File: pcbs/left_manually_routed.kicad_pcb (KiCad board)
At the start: 2 copper layers, 123.2 x 93.2 mm, 27 parts

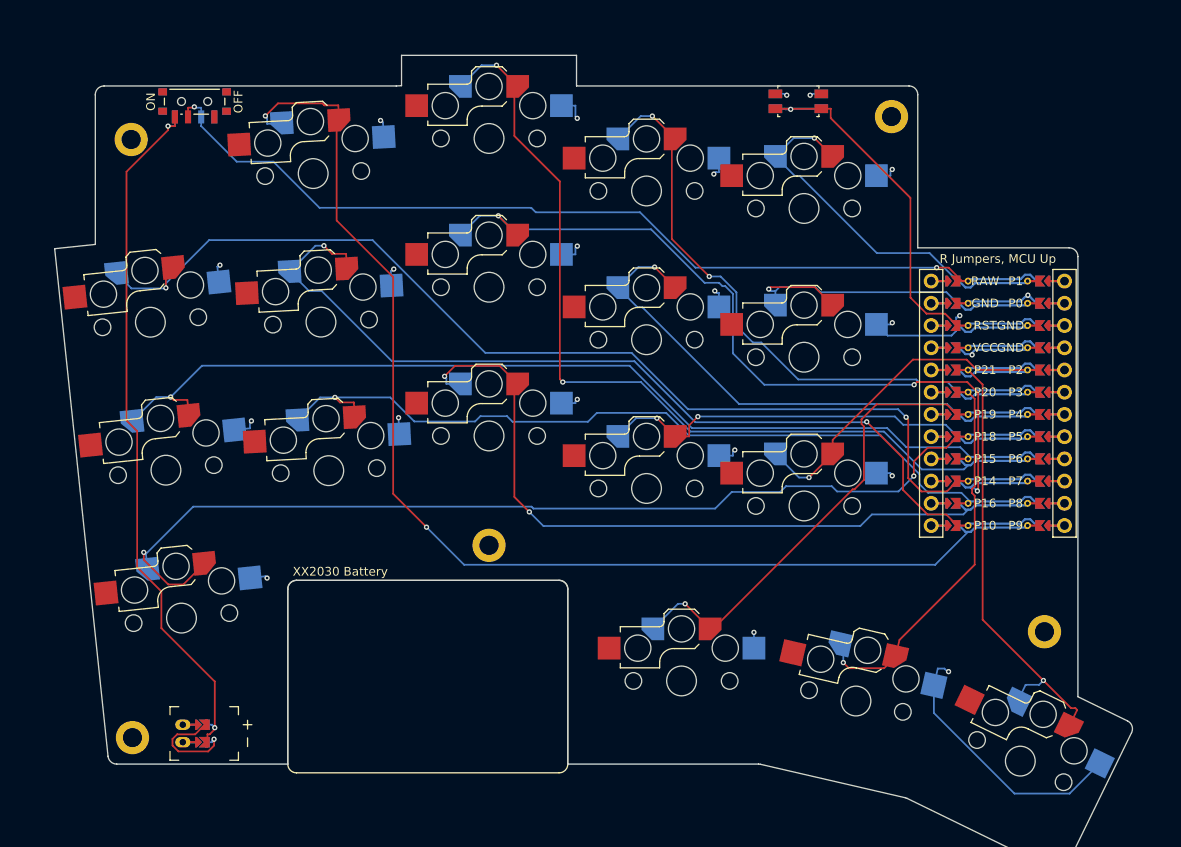
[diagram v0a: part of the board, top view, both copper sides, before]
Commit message: Update manually routed pcb and export model
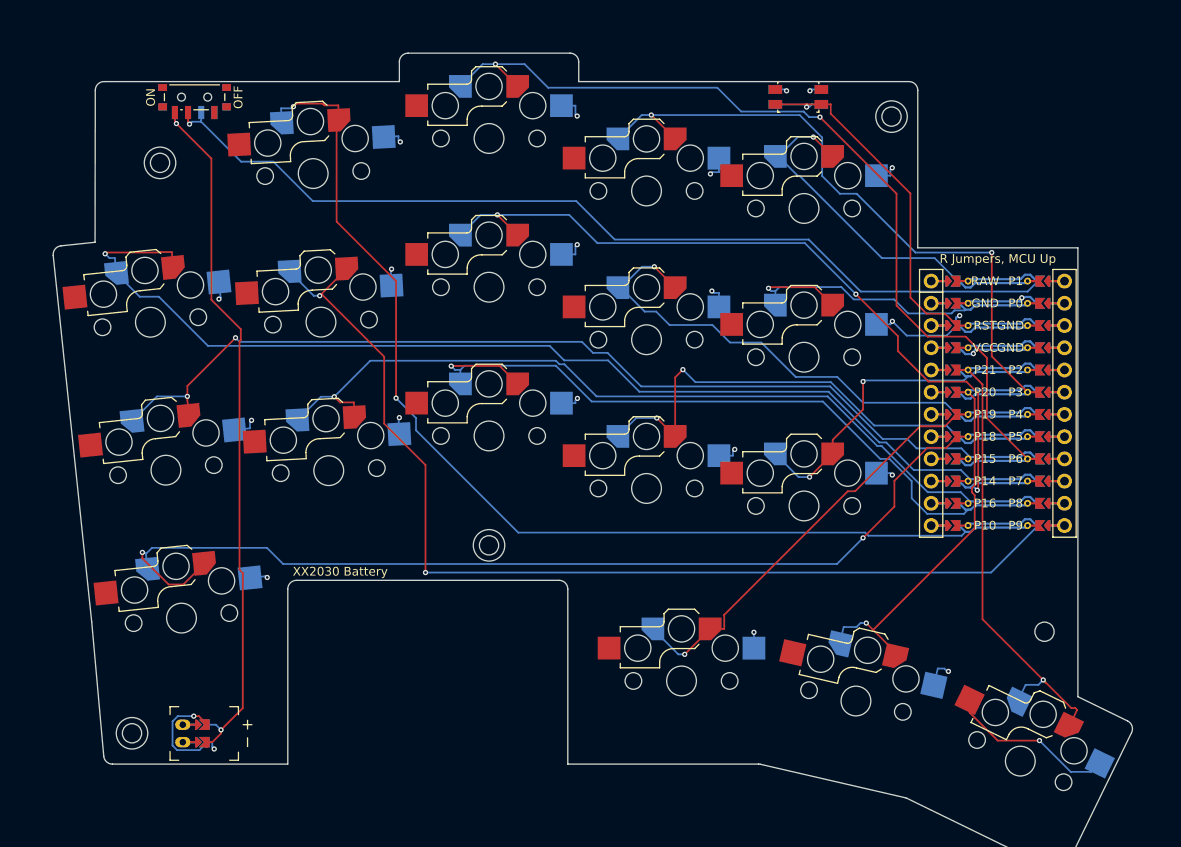
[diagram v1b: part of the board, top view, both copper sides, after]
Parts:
- removed H1, H2, H3, H4, H5: , ceoloide:mounting_hole_plated
- added MH1: , ceoloide:mounting_hole_npth, F.Cu at (97.5, 48.0)
- added MH2: , ceoloide:mounting_hole_npth, F.Cu at (181.1, 42.7)
- added MH3: , ceoloide:mounting_hole_npth, F.Cu at (94.3, 113.2)
- added MH4: , ceoloide:mounting_hole_npth, F.Cu at (135.1, 91.7)
- added MH5: , ceoloide:mounting_hole_npth, F.Cu at (198.6, 101.6)
- moved PWR1 0.50 mm to (101.5, 40.5)
- moved RST1 0.50 mm to (170.5, 40.4)
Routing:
- net P10: track 110.3 -> 128.1 mm
- net P9: track 139.7 -> 127.7 mm
- net P3: track 72.6 -> 84.6 mm
- net RAW: track 109.2 -> 118.2 mm, vias 2 -> 1
- net P5: track 53.3 -> 61.0 mm
- net GND: track 123.3 -> 116.5 mm, vias 23 -> 25
- net P2: track 47.1 -> 40.8 mm, vias 1 -> 2
- net P19: track 62.8 -> 58.3 mm
- net P6: track 105.6 -> 109.9 mm
- net P7: track 98.2 -> 95.0 mm
- net P18: track 122.1 -> 123.9 mm
- net P15: track 116.7 -> 118.4 mm, vias 1 -> 2
- net P0: track 42.7 -> 44.3 mm
- net P16: track 99.1 -> 100.7 mm
- net P14: track 128.5 -> 130.0 mm, vias 2 -> 1
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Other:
- board size 123.2 x 93.2 mm -> 123.3 x 93.5 mm
